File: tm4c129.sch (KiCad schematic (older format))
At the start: 15 parts, among them U1 TM4C1294NCPDTGOOD, Y1 Crystal_GND24

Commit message: updates
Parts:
- R5: footprint (none) -> Resistor_SMD:R_0603_1608Metric
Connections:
- net ~ENABLE: now also U1.31 (PH2)
- net ~INHIBIT: now also U1.32 (PH3)
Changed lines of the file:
@@
 EESchema Schematic File Version 4
+LIBS:Raptor2000-cache
 EELAYER 29 0
 EELAYER END
@@
 Wire Wire Line
 	2950 4000 3050 4000
-$Comp
-L Exodus_Microcontrollers:TM4C1294NCPDTGOOD-WRaptor1201-A-eagle-import U1
-U 1 1 5C7FA546
-P 5450 4150
-AR Path="/5C7FA546" Ref="U1"  Part="1"
-AR Path="/5C80AE96/5C7FA546" Ref="U1"  Part="1"
-F 0 "U1" H 5450 7536 59  0000 C CNN
-F 1 "TM4C1294NCPDTGOOD" H 5450 7431 59  0000 C CNN
-F 2 "Package_QFP:TQFP-128_14x14mm_P0.4mm" H 5450 4150 50  0001 C CNN
-F 3 "" H 5450 4150 50  0001 C CNN
-	1    5450 4150
-	1    0    0    -1
-$EndComp
 Wire Wire Line
 	4250 3050 4200 3050
@@
 Wire Wire Line
 	3900 5050 4250 5050
-Text HLabel 9450 1300 0    50   Input ~ 0
+Text HLabel 6900 5950 2    50   Input ~ 0
 ~ENABLE
-Text HLabel 9450 1450 0    50   Input ~ 0
+Text HLabel 6900 5850 2    50   Input ~ 0
 ~INHIBIT
-Text HLabel 9450 1600 0    50   Input ~ 0
+Text HLabel 7600 3200 0    50   Input ~ 0
 ~SYSRESET
 Wire Wire Line
@@
 F 0 "R5" H 7159 1246 50  0000 L CNN
 F 1 "R_Small" H 7159 1155 50  0000 L CNN
-F 2 "" H 7100 1200 50  0001 C CNN
+F 2 "Resistor_SMD:R_0603_1608Metric" H 7100 1200 50  0001 C CNN
 F 3 "~" H 7100 1200 50  0001 C CNN
 	1    7100 1200
@@
 	1    0    0    -1
 $EndComp
+$Comp
+L Exodus_Microcontrollers:TM4C1294NCPDTGOOD-WRaptor1201-A-eagle-import U1
+U 1 1 5C7FA546
+P 5450 4150
+AR Path="/5C7FA546" Ref="U1"  Part="1"
+AR Path="/5C80AE96/5C7FA546" Ref="U1"  Part="1"
+F 0 "U1" H 5450 7536 59  0000 C CNN
+F 1 "TM4C1294NCPDTGOOD" H 5450 7431 59  0000 C CNN
+F 2 "Package_QFP:TQFP-128_14x14mm_P0.4mm" H 5450 4150 50  0001 C CNN
+F 3 "" H 5450 4150 50  0001 C CNN
+	1    5450 4150
+	1    0    0    -1
+$EndComp
+Wire Wire Line
+	6650 5950 6900 5950
+Wire Wire Line
+	6650 5850 6900 5850
 $EndSCHEMATC

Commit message: fixing some unnamed nets.
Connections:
- net OSC1_R: now reaches C4.2, R1.2, Y1.3
- net VDDC: now reaches C5.1, C7.1, C9.1, U1.115 (VDDC), U1.87 (VDDC@1)
- net R_BIAS: now reaches R2.1, U1.59 (RBIAS)
- net RST: now reaches R5.2, U1.70 (RST)
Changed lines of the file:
@@
 Wire Wire Line
 	6650 5850 6900 5850
+Text Label 3550 2650 0    50   ~ 0
+VDDC
+Text Label 6850 1350 0    50   ~ 0
+RST
+Text Label 6850 1450 0    50   ~ 0
+R_BIAS
+Text Label 3300 4400 0    50   ~ 0
+OSC1_R
 $EndSCHEMATC

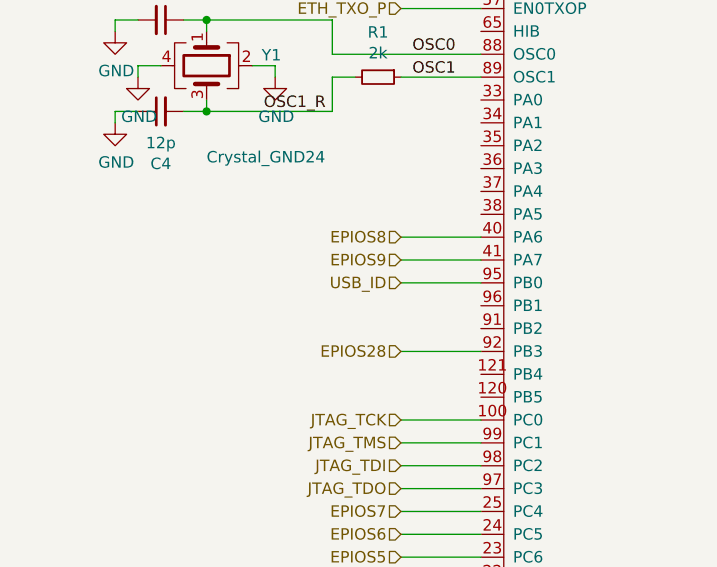
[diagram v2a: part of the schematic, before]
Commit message: Added usb id and usb vbus pins to tm4c circuit. Unconnected on main backplane connector.
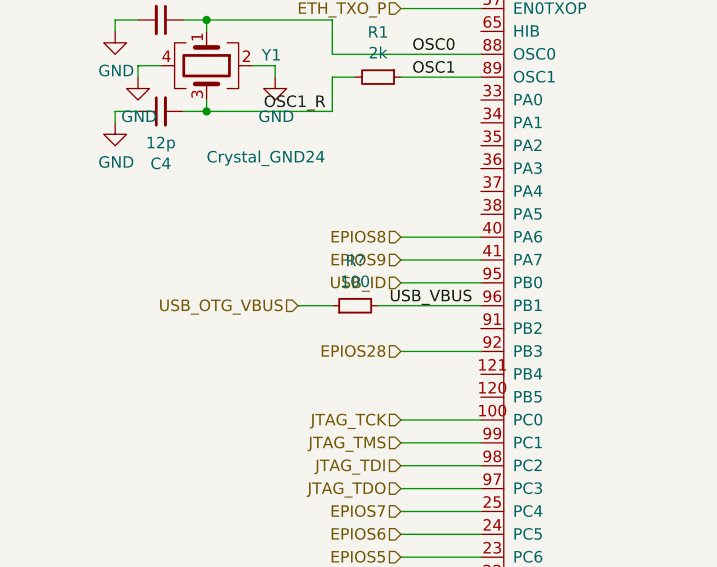
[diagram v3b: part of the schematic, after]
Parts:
- added R?: 100, Resistor_SMD:R_0603_1608Metric, symbol Device:R_Small
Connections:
- net USB_VBUS: now reaches U1.96 (PB1)
- net USB_VBUS: now also R?.2
- new net USB_OTG_VBUS: R?.1
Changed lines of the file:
@@
 Text Label 3300 4400 0    50   ~ 0
 OSC1_R
+Text HLabel 3450 5250 0    50   Input ~ 0
+USB_OTG_VBUS
+$Comp
+L Device:R_Small R?
+U 1 1 5CF618A1
+P 3700 5250
+F 0 "R?" V 3896 5250 50  0000 C CNN
+F 1 "100" V 3805 5250 50  0000 C CNN
+F 2 "Resistor_SMD:R_0603_1608Metric" H 3700 5250 50  0001 C CNN
+F 3 "~" H 3700 5250 50  0001 C CNN
+	1    3700 5250
+	0    -1   -1   0
+$EndComp
+Wire Wire Line
+	3450 5250 3600 5250
+Text Label 3850 5250 0    50   ~ 0
+USB_VBUS
+Wire Wire Line
+	3800 5250 4250 5250
 $EndSCHEMATC

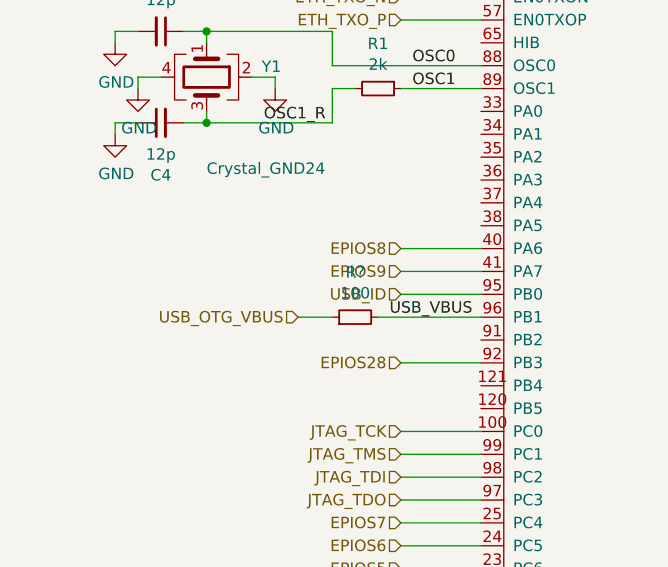
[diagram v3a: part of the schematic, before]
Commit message: Changed USB ID and VBUS resistors.
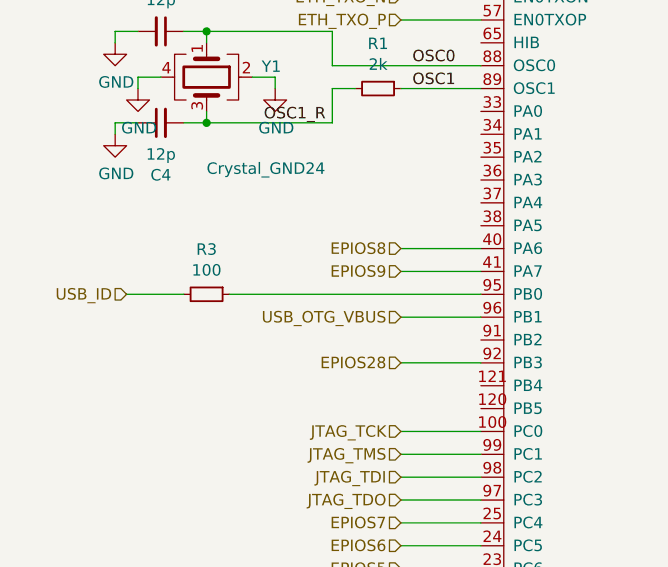
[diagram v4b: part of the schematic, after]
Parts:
- removed R?: 100, Resistor_SMD:R_0603_1608Metric, symbol Device:R_Small
- added R3: 100, symbol Device:R_Small
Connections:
- net USB_VBUS is gone; now on net USB_OTG_VBUS: U1.96 (PB1)
- net USB_ID: now also R3.2; no longer U1.95 (PB0)
- new net: R3.1, U1.95 (PB0)
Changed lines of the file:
@@
 EESchema Schematic File Version 4
-LIBS:Raptor2000-cache
-EELAYER 29 0
+EELAYER 26 0
 EELAYER END
 $Descr A4 11693 8268
@@
 Text HLabel 6900 4150 2    50   Input ~ 0
 USB_D_P
-Wire Wire Line
-	4250 5150 3900 5150
-Text HLabel 3900 5150 0    50   Input ~ 0
+Text HLabel 2700 5150 0    50   Input ~ 0
 USB_ID
 $Comp
@@
 Text Label 3300 4400 0    50   ~ 0
 OSC1_R
-Text HLabel 3450 5250 0    50   Input ~ 0
+Text HLabel 3900 5250 0    50   Input ~ 0
 USB_OTG_VBUS
-$Comp
-L Device:R_Small R?
-U 1 1 5CF618A1
-P 3700 5250
-F 0 "R?" V 3896 5250 50  0000 C CNN
-F 1 "100" V 3805 5250 50  0000 C CNN
-F 2 "Resistor_SMD:R_0603_1608Metric" H 3700 5250 50  0001 C CNN
-F 3 "~" H 3700 5250 50  0001 C CNN
-	1    3700 5250
-	0    -1   -1   0
-$EndComp
-Wire Wire Line
-	3450 5250 3600 5250
-Text Label 3850 5250 0    50   ~ 0
-USB_VBUS
-Wire Wire Line
-	3800 5250 4250 5250
+Wire Wire Line
+	3900 5250 4250 5250
+$Comp
+L Device:R_Small R3
+U 1 1 5CFE983D
+P 3050 5150
+F 0 "R3" V 2854 5150 50  0000 C CNN
+F 1 "100" V 2945 5150 50  0000 C CNN
+F 2 "" H 3050 5150 50  0001 C CNN
+F 3 "~" H 3050 5150 50  0001 C CNN
+	1    3050 5150
+	0    1    1    0
+$EndComp
+Wire Wire Line
+	3150 5150 4250 5150
+Wire Wire Line
+	2700 5150 2950 5150
 $EndSCHEMATC

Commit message: initial implementation of vbatt for RTC.
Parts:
- added BT1: Battery_Cell, symbol Device:Battery_Cell
- added C11, C12: 12p, Capacitor_SMD:C_0603_1608Metric, symbol Device:C_Small
- added C13: 0.1, Capacitor_SMD:C_0603_1608Metric, symbol Device:C_Small
- added R4: 2k, Resistor_SMD:R_0603_1608Metric, symbol Device:R_Small
- added R6: 51, Resistor_SMD:R_0603_1608Metric, symbol Device:R_Small
- added Y2: Crystal_GND24, Crystal:Crystal_SMD_3225-4Pin_3.2x2.5mm, symbol Device:Crystal_GND24
- R3: footprint (none) -> Resistor_SMD:R_0603_1608Metric
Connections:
- net labels added: Batt_Pos, VBat, XOSC0, XOSC1, XOSC1_R
- wire segments 152 -> 182
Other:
- moved on the sheet: C10, C2, C6, C8

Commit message: added nand flash, removed sd card. finished rtc circuit. added leds
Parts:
- removed R4: 2k, Resistor_SMD:R_0603_1608Metric, symbol Device:R_Small
- removed Y2: Crystal_GND24, Crystal:Crystal_SMD_3225-4Pin_3.2x2.5mm, symbol Device:Crystal_GND24
- added C15, C16: 0.1, symbol Device:C_Small
- added D1, D2, D3, D4, D6, D7: LED, symbol Device:LED
- added D5: LED, LED_SMD:LED_0603_1608Metric, symbol Device:LED
- added R10: 330, Resistor_SMD:R_0603_1608Metric, symbol Device:R_Small
- added R11, R12, R7, R8, R9: 330, symbol Device:R_Small
- added R13, R15, R16: 49.9, symbol Device:R_Small
- added R14: 49.4, symbol Device:R_Small
- added Y2: Crystal, symbol Device:Crystal
- C10: value C_Small -> 0.1
- C7: value C_Small -> 0.1u
- R5: value R_Small -> 330; footprint Resistor_SMD:R_0603_1608Metric -> (none)
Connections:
- net labels added: EPIOS131, EPIOS[0..31], ETH_LED0_CATHODE, ETH_LED1_CATHODE, PWR_LED_CATHODE, SSI2Clk, SSI2Fss, SSI2XDAT0, SSI2XDAT1, SSI2XDAT2, SSI2XDAT3, USB_ID_R, USER_LED0, USER_LED0_CATHODE, USER_LED1, USER_LED1_CATHOD, USER_LED2, USER_LED3
- net labels removed: EPIOS31, RST, SPI_DAT2, SPI_DAT3, SPI_MISO, SPI_MOSI, SPI_SCLK, SPI_SS, XOSC1_R
- wire segments 182 -> 222
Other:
- moved on the sheet: C1, C10, C11, C12, C13, C2, C3, C4, C5, C6, C7, C8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

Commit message: fixed misnamed EPI nets.
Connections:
- net labels added: EPI029, EPI030, EPI0S0, EPI0S1, EPI0S10, EPI0S11, EPI0S12, EPI0S13, EPI0S14, EPI0S15, EPI0S16, EPI0S17, EPI0S18, EPI0S19, EPI0S2, EPI0S28, EPI0S3, EPI0S31, EPI0S4, EPI0S5, EPI0S6, EPI0S7, EPI0S8, EPI0S9, EPI0S[0..31]
- net labels removed: EPIOS0, EPIOS1, EPIOS10, EPIOS11, EPIOS12, EPIOS13, EPIOS131, EPIOS14, EPIOS15, EPIOS16, EPIOS17, EPIOS18, EPIOS19, EPIOS2, EPIOS28, EPIOS29, EPIOS3, EPIOS30, EPIOS4, EPIOS5, EPIOS6, EPIOS7, EPIOS8, EPIOS9, EPIOS[0..31]
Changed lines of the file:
@@
 SSI2XDAT1
-Wire Wire Line
-	5400 2350 5150 2350
-Wire Wire Line
-	5400 2250 5150 2250
-Text HLabel 5400 2350 2    50   Input ~ 0
-EPIOS29
-Text HLabel 5400 2250 2    50   Input ~ 0
-EPIOS30
 Wire Wire Line
 	2750 6050 2400 6050
@@
 	5900 6350 6000 6450
 Text Label 5400 3650 0    50   ~ 0
-EPIOS12
+EPI0S12
 Text Label 5400 3750 0    50   ~ 0
-EPIOS13
+EPI0S13
 Text Label 5400 3850 0    50   ~ 0
-EPIOS14
+EPI0S14
 Text Label 5400 3950 0    50   ~ 0
-EPIOS15
+EPI0S15
 Text Label 5400 4450 0    50   ~ 0
-EPIOS19
+EPI0S19
 Text Label 5400 4550 0    50   ~ 0
-EPIOS18
+EPI0S18
 Text Label 5400 4650 0    50   ~ 0
-EPIOS17
+EPI0S17
 Text Label 5400 4750 0    50   ~ 0
-EPIOS16
+EPI0S16
 Text Label 5400 5050 0    50   ~ 0
-EPIOS131
+EPI0S31
 Text Label 5400 5250 0    50   ~ 0
-EPIOS3
+EPI0S3
 Text Label 5400 5350 0    50   ~ 0
-EPIOS2
+EPI0S2
 Text Label 5400 5450 0    50   ~ 0
-EPIOS1
+EPI0S1
 Text Label 5400 5550 0    50   ~ 0
-EPIOS0
+EPI0S0
 Text Label 5400 6250 0    50   ~ 0
-EPIOS10
+EPI0S10
 Text Label 5400 6350 0    50   ~ 0
-EPIOS11
+EPI0S11
 Wire Bus Line
 	6000 7600 1700 7600
@@
 	1700 5550 1800 5450
 Text Label 1950 4950 0    50   ~ 0
-EPIOS8
+EPI0S8
 Text Label 1950 6450 0    50   ~ 0
-EPIOS4
+EPI0S4
 Text Label 1950 6350 0    50   ~ 0
-EPIOS5
+EPI0S5
 Text Label 1950 6250 0    50   ~ 0
-EPIOS6
+EPI0S6
 Text Label 1950 6150 0    50   ~ 0
-EPIOS7
+EPI0S7
 Text Label 1950 5450 0    50   ~ 0
-EPIOS28
+EPI0S28
 Text Label 1950 5050 0    50   ~ 0
-EPIOS9
+EPI0S9
 Wire Bus Line
 	1700 4850 1550 4850
@@
 JTAG_TCK
 Text HLabel 1550 4850 0    50   Input ~ 0
-EPIOS[0..31]
+EPI0S[0..31]
 Wire Wire Line
 	5150 1050 5900 1050
@@
 Wire Wire Line
 	5450 1500 5450 1450
+Wire Wire Line
+	5150 2250 5900 2250
+Wire Wire Line
+	5150 2350 5900 2350
 Wire Bus Line
 	1700 4850 1700 7600
 Wire Bus Line
-	6000 3550 6000 7600
+	6000 2200 6000 7600
+Entry Wire Line
+	5900 2250 6000 2350
+Entry Wire Line
+	5900 2350 6000 2450
+Text Label 5450 2250 0    50   ~ 0
+EPI030
+Text Label 5450 2350 0    50   ~ 0
+EPI029
 $EndSCHEMATC

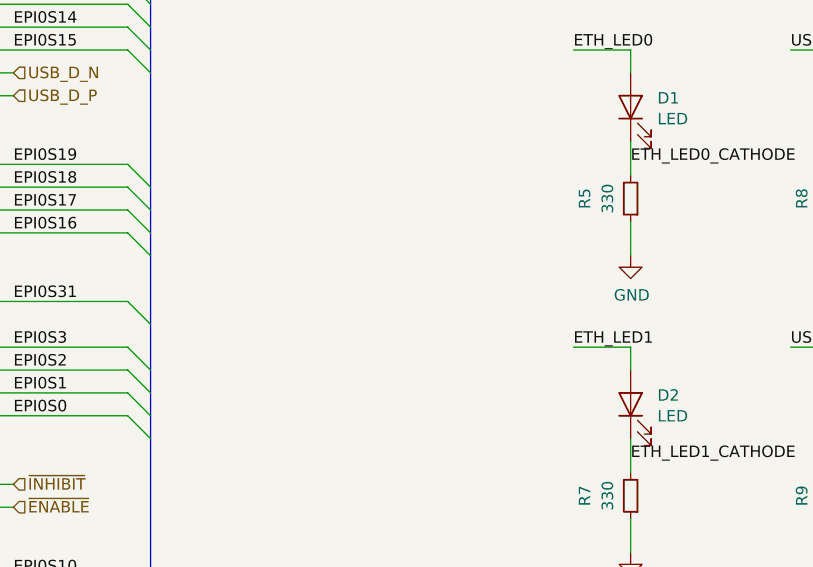
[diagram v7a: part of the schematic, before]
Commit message: added a note about EPI signal drive strength.
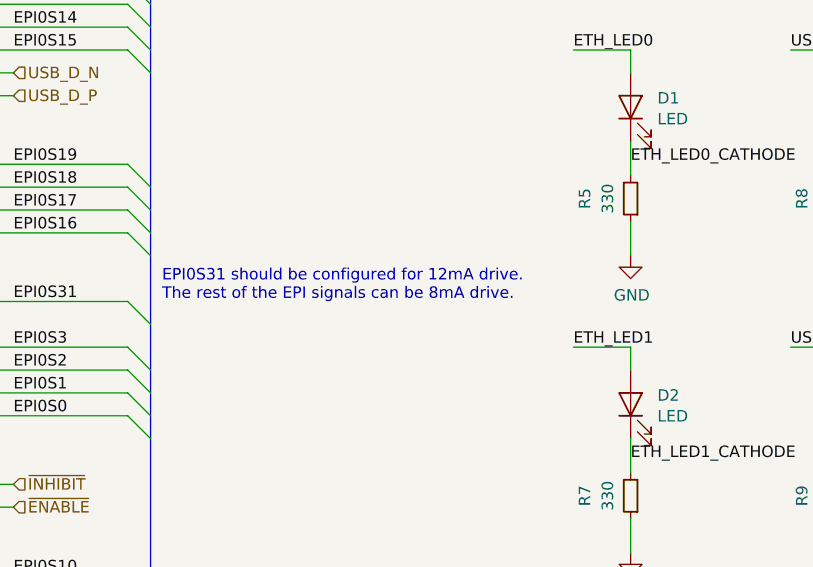
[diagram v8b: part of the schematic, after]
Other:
- note added: "EPI0S31 should be configured for 12mA drive. \nThe rest of the EPI signals can be 8mA drive."
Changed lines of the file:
@@
 Wire Wire Line
 	5150 2350 5900 2350
-Wire Bus Line
-	1700 4850 1700 7600
-Wire Bus Line
-	6000 2200 6000 7600
 Entry Wire Line
 	5900 2250 6000 2350
@@
 Text Label 5450 2350 0    50   ~ 0
 EPI029
+Wire Bus Line
+	1700 4850 1700 7600
+Wire Bus Line
+	6000 2200 6000 7600
+Text Notes 6050 5050 0    50   ~ 0
+EPI0S31 should be configured for 12mA drive. \nThe rest of the EPI signals can be 8mA drive.
 $EndSCHEMATC
